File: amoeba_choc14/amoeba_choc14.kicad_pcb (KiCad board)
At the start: 2 copper layers, 14 x 16 mm, 8 parts, among them J1 Conn_01x01_Pin, J2 Conn_01x01_Pin, J3 Conn_01x01_Pin, J4 Conn_01x01_Pin, SW1 SW_SPST

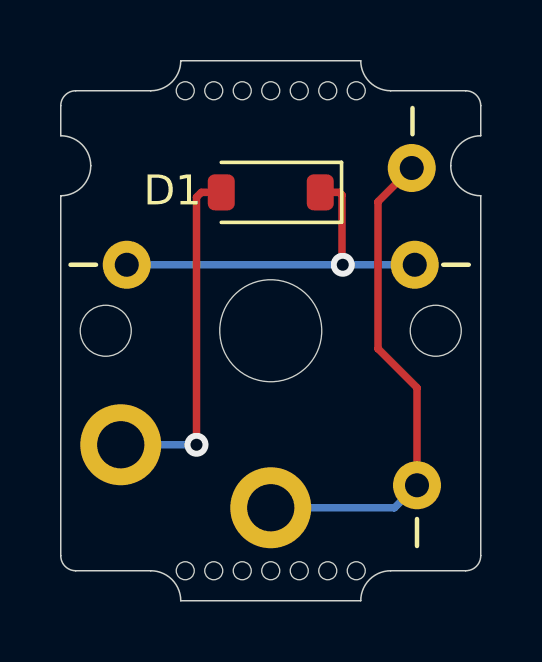
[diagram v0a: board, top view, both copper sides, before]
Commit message: fix: label vs mask, update dioode from lib
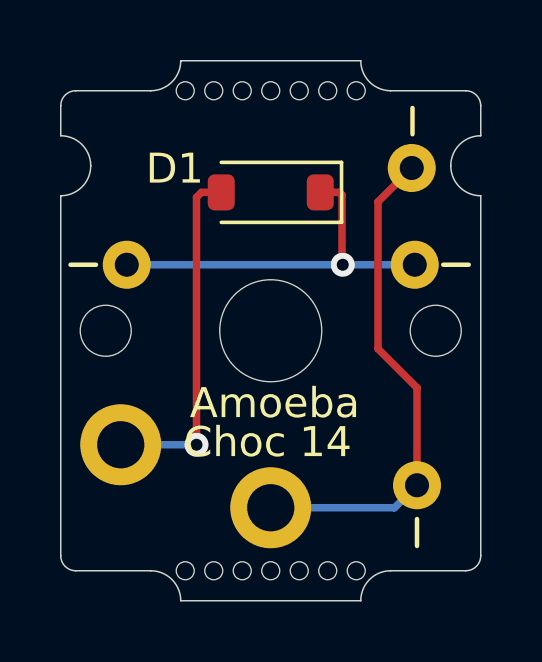
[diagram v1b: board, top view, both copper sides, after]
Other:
- board text added: "Amoeba"
- board text added: "Choc 14"
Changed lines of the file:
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@@
 		(tags "SOD-123")
 		(property "Reference" "D1"
-			(at 3.275 0.0625 180)
+			(at 3.2 0.7875 180)
 			(layer "F.SilkS")
 			(effects
@@
 		)
 		(property "Value" "1N4148"
-			(at 1.425 1.6375 180)
+			(at 1.3 2.1875 180)
 			(layer "F.Fab")
 			(effects
@@
 		)
 		(property "Footprint" "Diode_SMD:D_SOD-123"
-			(at 0 0 0)
-			(unlocked yes)
-			(layer "B.Fab")
-			(hide yes)
-			(effects
-				(font
-					(size 1.27 1.27)
-				)
-				(justify mirror)
+			(at 0 0 180)
+			(unlocked yes)
+			(layer "F.Fab")
+			(hide yes)
+			(effects
+				(font
+					(size 1.27 1.27)
+				)
 			)
 		)
 		(property "Datasheet" "https://assets.nexperia.com/documents/data-sheet/1N4148_1N4448.pdf"
-			(at 0 0 0)
-			(unlocked yes)
-			(layer "B.Fab")
-			(hide yes)
-			(effects
-				(font
-					(size 1.27 1.27)
-				)
-				(justify mirror)
+			(at 0 0 180)
+			(unlocked yes)
+			(layer "F.Fab")
+			(hide yes)
+			(effects
+				(font
+					(size 1.27 1.27)
+				)
 			)
 		)
 		(property "Description" ""
-			(at 0 0 0)
-			(unlocked yes)
-			(layer "B.Fab")
-			(hide yes)
-			(effects
-				(font
-					(size 1.27 1.27)
-				)
-				(justify mirror)
+			(at 0 0 180)
+			(unlocked yes)
+			(layer "F.Fab")
+			(hide yes)
+			(effects
+				(font
+					(size 1.27 1.27)
+				)
 			)
 		)
@@
 			)
 		)
-		(property ki_fp_filters "D*DO?35*")
-		(sheetname "Root")
-		(sheetfile "amoeba_choc14.kicad_sch")
 		(attr smd)
 		(fp_line
-			(start 1.65 1)
+			(start -2.36 1)
+			(end 1.65 1)
+			(stroke
+				(width 0.12)
+				(type solid)
+			)
+			(layer "F.SilkS")
+		)
+		(fp_line
+			(start -2.36 -1)
+			(end 1.65 -1)
+			(stroke
+				(width 0.12)
+				(type solid)
+			)
+			(layer "F.SilkS")
+		)
+		(fp_line
+			(start -2.36 -1)
 			(end -2.36 1)
 			(stroke
@@
 		)
 		(fp_line
-			(start 1.65 -1)
-			(end -2.36 -1)
-			(stroke
-				(width 0.12)
-				(type solid)
-			)
-			(layer "F.SilkS")
-		)
-		(fp_line
-			(start -2.36 1)
-			(end -2.36 -1)
-			(stroke
-				(width 0.12)
-				(type solid)
-			)
-			(layer "F.SilkS")
-		)
-		(fp_line
 			(start 2.35 1.15)
+			(end -2.35 1.15)
+			(stroke
+				(width 0.05)
+				(type solid)
+			)
+			(layer "F.CrtYd")
+		)
+		(fp_line
+			(start 2.35 -1.15)
+			(end 2.35 1.15)
+			(stroke
+				(width 0.05)
+				(type solid)
+			)
+			(layer "F.CrtYd")
+		)
+		(fp_line
+			(start -2.35 -1.15)
 			(end 2.35 -1.15)
 			(stroke
@@
 		)
 		(fp_line
-			(start 2.35 -1.15)
-			(end -2.35 -1.15)
+			(start -2.35 -1.15)
+			(end -2.35 1.15)
 			(stroke
 				(width 0.05)
@@
 		)
 		(fp_line
-			(start -2.35 1.15)
-			(end 2.35 1.15)
-			(stroke
-				(width 0.05)
-				(type solid)
-			)
-			(layer "F.CrtYd")
-		)
-		(fp_line
-			(start -2.35 1.15)
-			(end -2.35 -1.15)
-			(stroke
-				(width 0.05)
-				(type solid)
-			)
-			(layer "F.CrtYd")
-		)
-		(fp_line
 			(start 1.4 0.9)
+			(end -1.4 0.9)
+			(stroke
+				(width 0.1)
+				(type solid)
+			)
+			(layer "F.Fab")
+		)
+		(fp_line
+			(start 1.4 -0.9)
+			(end 1.4 0.9)
+			(stroke
+				(width 0.1)
+				(type solid)
+			)
+			(layer "F.Fab")
+		)
+		(fp_line
+			(start 0.25 0.4)
+			(end -0.35 0)
+			(stroke
+				(width 0.1)
+				(type solid)
+			)
+			(layer "F.Fab")
+		)
+		(fp_line
+			(start 0.25 0)
+			(end 0.75 0)
+			(stroke
+				(width 0.1)
+				(type solid)
+			)
+			(layer "F.Fab")
+		)
+		(fp_line
+			(start 0.25 -0.4)
+			(end 0.25 0.4)
+			(stroke
+				(width 0.1)
+				(type solid)
+			)
+			(layer "F.Fab")
+		)
+		(fp_line
+			(start -0.35 0)
+			(end 0.25 -0.4)
+			(stroke
+				(width 0.1)
+				(type solid)
+			)
+			(layer "F.Fab")
+		)
+		(fp_line
+			(start -0.35 0)
+			(end -0.35 0.55)
+			(stroke
+				(width 0.1)
+				(type solid)
+			)
+			(layer "F.Fab")
+		)
+		(fp_line
+			(start -0.35 0)
+			(end -0.35 -0.55)
+			(stroke
+				(width 0.1)
+				(type solid)
+			)
+			(layer "F.Fab")
+		)
+		(fp_line
+			(start -0.75 0)
+			(end -0.35 0)
+			(stroke
+				(width 0.1)
+				(type solid)
+			)
+			(layer "F.Fab")
+		)
+		(fp_line
+			(start -1.4 0.9)
+			(end -1.4 -0.9)
+			(stroke
+				(width 0.1)
+				(type solid)
+			)
+			(layer "F.Fab")
+		)
+		(fp_line
+			(start -1.4 -0.9)
 			(end 1.4 -0.9)
 			(stroke
@@
 			(layer "F.Fab")
 		)
-		(fp_line
-			(start 1.4 -0.9)
-			(end -1.4 -0.9)
-			(stroke
-				(width 0.1)
-				(type solid)
-			)
-			(layer "F.Fab")
-		)
-		(fp_line
-			(start 0.75 0)
-			(end 0.25 0)
-			(stroke
-				(width 0.1)
-				(type solid)
-			)
-			(layer "F.Fab")
-		)
-		(fp_line
-			(start 0.25 0.4)
-			(end 0.25 -0.4)
-			(stroke
-				(width 0.1)
-				(type solid)
-			)
-			(layer "F.Fab")
-		)
-		(fp_line
-			(start 0.25 -0.4)
-			(end -0.35 0)
-			(stroke
-				(width 0.1)
-				(type solid)
-			)
-			(layer "F.Fab")
-		)
-		(fp_line
-			(start -0.35 0.55)
-			(end -0.35 0)
-			(stroke
-				(width 0.1)
-				(type solid)
-			)
-			(layer "F.Fab")
-		)
-		(fp_line
-			(start -0.35 0)
-			(end 0.25 0.4)
-			(stroke
-				(width 0.1)
-				(type solid)
-			)
-			(layer "F.Fab")
-		)
-		(fp_line
-			(start -0.35 0)
-			(end -0.75 0)
-			(stroke
-				(width 0.1)
-				(type solid)
-			)
-			(layer "F.Fab")
-		)
-		(fp_line
-			(start -0.35 -0.55)
-			(end -0.35 0)
-			(stroke
-				(width 0.1)
-				(type solid)
-			)
-			(layer "F.Fab")
-		)
-		(fp_line
-			(start -1.4 0.9)
-			(end 1.4 0.9)
-			(stroke
-				(width 0.1)
-				(type solid)
-			)
-			(layer "F.Fab")
-		)
-		(fp_line
-			(start -1.4 -0.9)
-			(end -1.4 0.9)
-			(stroke
-				(width 0.1)
-				(type solid)
-			)
-			(layer "F.Fab")
-		)
 		(fp_text user "${REFERENCE}"
-			(at 3.275 0.0875 180)
+			(at 0 -2 180)
 			(layer "F.Fab")
 			(effects
@@
 			(pintype "passive")
 		)
-		(model "${KICAD6_3DMODEL_DIR}/Diode_SMD.3dshapes/D_SOD-123.wrl"
+		(model "${KICAD8_3DMODEL_DIR}/Diode_SMD.3dshapes/D_SOD-123.wrl"
 			(offset
 				(xyz 0 0 0)
@@
 		(layer "Edge.Cuts")
 	)
+	(gr_text "Choc 14"
+		(at 127.1 114.3 0)
+		(layer "F.SilkS")
+		(effects
+			(font
+				(size 1 1)
+				(thickness 0.15)
+			)
+			(justify left bottom)
+		)
+	)
+	(gr_text "Amoeba"
+		(at 127.3 113 0)
+		(layer "F.SilkS")
+		(effects
+			(font
+				(size 1 1)
+				(thickness 0.15)
+			)
+			(justify left bottom)
+		)
+	)
 	(gr_text "Outer ticks are choc spacing, 18 x 17 \nInner ticks are clip width x body depth, 14.5 x 13.8\nBlue outline is switch lower body, 13.8 x 13.8"
 		(at 112.25 127.75 0)
@@
 		)
 	)
-	(gr_text_box "Amoeba\nChoc 14"
-		(start 126.275 110.9)
-		(end 134.325 114.425)
-		(layer "F.SilkS")
-		(effects
-			(font
-				(size 1 1)
-				(thickness 0.15)
-			)
-			(justify left top)
-		)
-		(border no)
-		(stroke
-			(width 0)
-			(type solid)
-		)
-	)
